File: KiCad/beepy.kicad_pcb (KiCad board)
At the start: 4 copper layers, 74 x 104 mm, 160 parts, among them J1 FDX0019B1, J10 FDX0019B1, J11 FDX0019B1, J12 FDX0019B1, J13 FDX0019B1, J14 FDX0019B1, J15 USB_C_Receptacle_USB2.0, J16 FDX0019B1, J17 FDX0019B1, J18 FDX0019B1, J19 FDX0019B1, J2 FDX0019B1, J20 FDX0019B1, J21 FDX0019B1, J23 FDX0019B1, J24 FDX0019B1, J25 FDX0019B1, J26 FDX0019B1, J27 FDX0019B1, J28 FDX0019B1, J29 FDX0019B1, J3 FDX0019B1, J30 FDX0019B1, J31 FDX0019B1, J32 FDX0019B1, J33 FDX0019B1, J34 FDX0019B1, J35 FDX0019B1, J36 FDX0019B1, J37 FDX0019B1, J38 FDX0019B1, J39 FDX0019B1, J4 FDX0019B1, J40 FDX0019B1, J41 FDX0019B1, J42 FDX0019B1, J43 Battery, J44 Header 1, J45 PRG_HEADER, J46 Header 2, J47 Header 3, J5 FDX0019B1, J6 FDX0019B1, J7 FDX0019B1, J8 FDX0019B1, J9 FDX0019B1, M1 MountingHole_2.5mm_Pad, M2 MountingHole_2.5mm_Pad, M3 MountingHole_2.5mm_Pad, M4 MountingHole_2.5mm_Pad, Q1 SI2301, Q2 SI2301, Q3 BSS138, Q4 BSS138, Q5 BSS138, Q6 BSS138, Q7 BSS138, Q8 BSS138, Q9 S8050, SW1 ON/OFF, SW2 Button, U1 TP4054, U2 TPS61090, U3 LS027B7DH01, U4 AP2112K-3.3, U5 GD25Q16xS, U6 RP2040, U7 ME6212C18M5G, U8 ME6212C28M5G, U9 BBQ20KBD, Y1 XYDBPCNANF-12MHZ

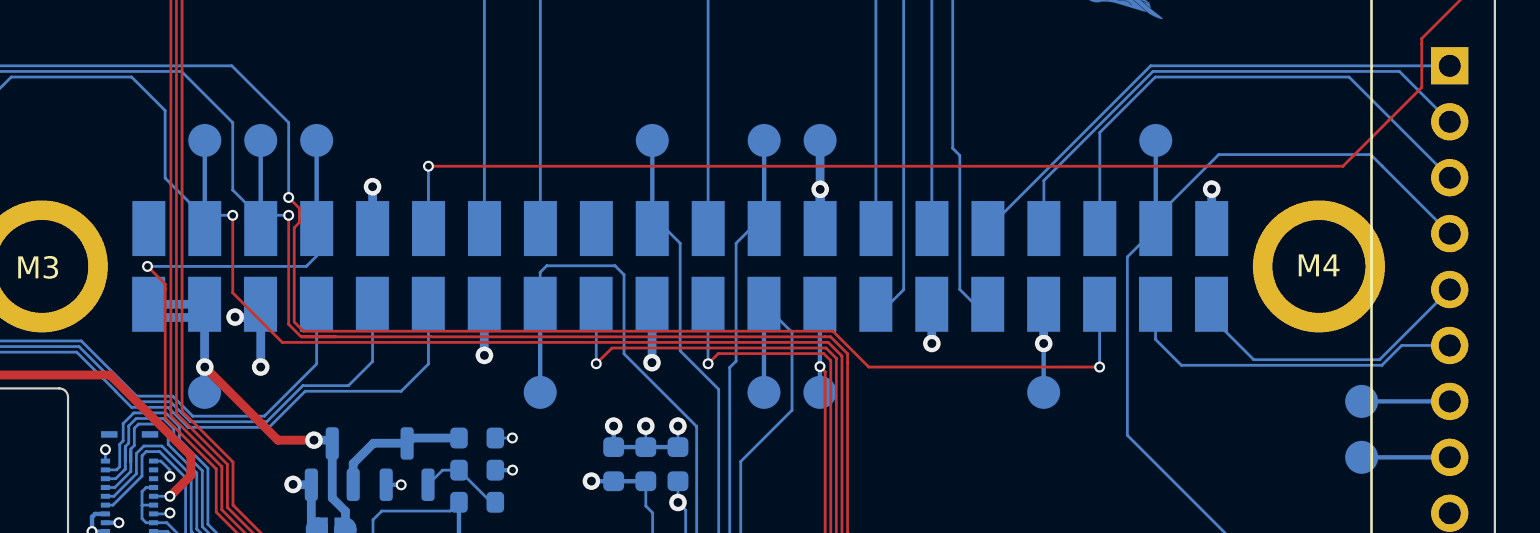
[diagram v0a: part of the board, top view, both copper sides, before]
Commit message: Importing to KiCAD 8 and using pin headers instead of springs
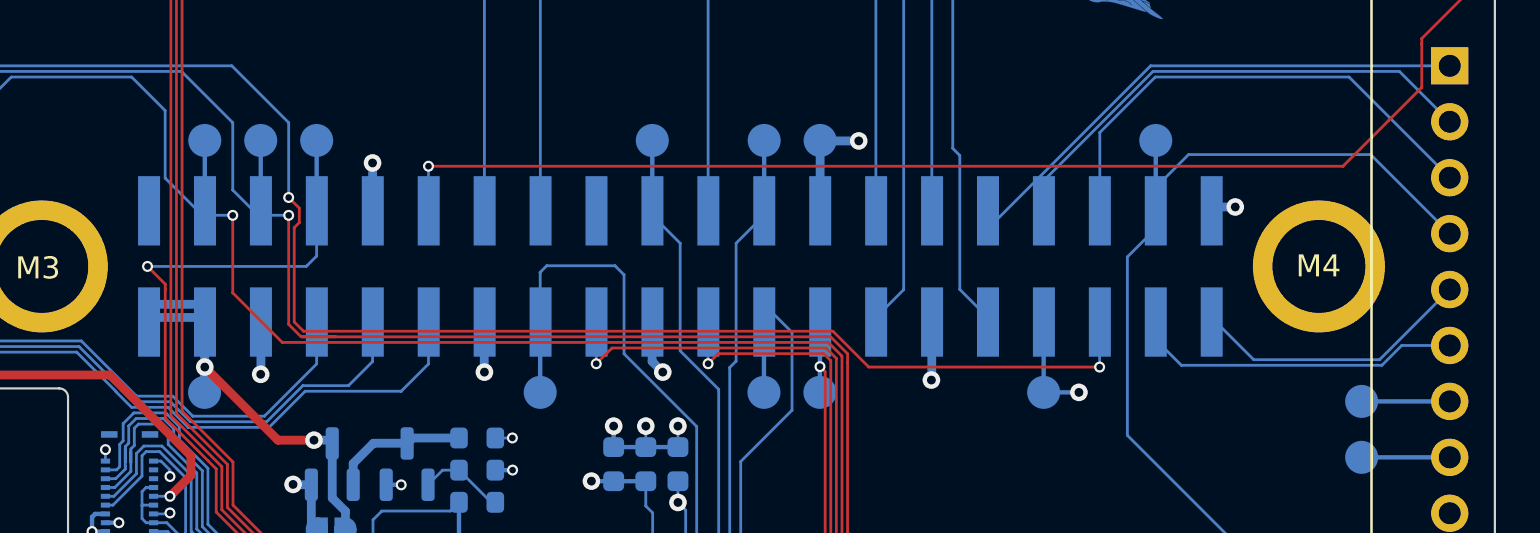
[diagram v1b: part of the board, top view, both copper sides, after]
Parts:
- removed J1, J10, J11, J12, J13, J14, J16, J17, J18, J19, J2, J20, J21, J23, J24, J25, J26, J27, J28, J29, J3, J30, J31, J32, J33, J34, J35, J36, J37, J38, J39, J4, J40, J41, J42, J5, J6, J7, J8, J9: FDX0019B1, beepy:FDX0019B1
- added J22: Pi Zero, Connector_PinHeader_2.54mm:PinHeader_2x20_P2.54mm_Vertical_SMD, B.Cu at (91.1, 69.2)
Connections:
- net /keyboard/BATT_ADC renamed /RP2040/BATT_ADC
- net /keyboard/COL1 renamed /RP2040/COL1
- net /keyboard/COL2 renamed /RP2040/COL2
- net /keyboard/COL3 renamed /RP2040/COL3
- net /keyboard/COL4 renamed /RP2040/COL4
- net /keyboard/COL5 renamed /RP2040/COL5
- net /keyboard/COL6 renamed /RP2040/COL6
- net /keyboard/COL7 renamed /RP2040/COL7
- net /keyboard/D+ renamed /RP2040/D+
- net /keyboard/D- renamed /RP2040/D-
- net /keyboard/KB_BL renamed /RP2040/KB_BL
- net /keyboard/Keyboard/TP_MOTION_1V8 renamed /RP2040/Keyboard/TP_MOTION_1V8
- net /keyboard/Keyboard/TP_RESET_1V8 renamed /RP2040/Keyboard/TP_RESET_1V8
- net /keyboard/Keyboard/TP_SCL_1V8 renamed /RP2040/Keyboard/TP_SCL_1V8
- net /keyboard/Keyboard/TP_SDA_1V8 renamed /RP2040/Keyboard/TP_SDA_1V8
- net /keyboard/Keyboard/TP_SHUTDOWN_1V8 renamed /RP2040/Keyboard/TP_SHUTDOWN_1V8
- net /keyboard/LED_B renamed /RP2040/LED_B
- net /keyboard/LED_G renamed /RP2040/LED_G
- net /keyboard/LED_R renamed /RP2040/LED_R
- net /keyboard/MIC renamed /RP2040/MIC
- net /keyboard/QSPI_SCLK renamed /RP2040/QSPI_SCLK
- net /keyboard/QSPI_SD0 renamed /RP2040/QSPI_SD0
- net /keyboard/QSPI_SD1 renamed /RP2040/QSPI_SD1
- net /keyboard/QSPI_SD2 renamed /RP2040/QSPI_SD2
- net /keyboard/QSPI_SD3 renamed /RP2040/QSPI_SD3
- net /keyboard/ROW1 renamed /RP2040/ROW1
- net /keyboard/ROW2 renamed /RP2040/ROW2
- net /keyboard/ROW3 renamed /RP2040/ROW3
- net /keyboard/ROW4 renamed /RP2040/ROW4
- net /keyboard/ROW5 renamed /RP2040/ROW5
- net /keyboard/ROW6 renamed /RP2040/ROW6
- net /keyboard/ROW7 renamed /RP2040/ROW7
- net /keyboard/TP_MOTION renamed /RP2040/TP_MOTION
- net /keyboard/TP_RESET renamed /RP2040/TP_RESET
- net /keyboard/TP_SCL renamed /RP2040/TP_SCL
- net /keyboard/TP_SDA renamed /RP2040/TP_SDA
- net /keyboard/TP_SHUTDOWN renamed /RP2040/TP_SHUTDOWN
- net /keyboard/~{QSPI_CS} renamed /RP2040/~{QSPI_CS}
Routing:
- net GND: track 104.3 -> 106.5 mm, vias 58 -> 57
- net /Pi_GPIO26: track 80.6 -> 81.4 mm
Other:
- board text added: "REF**"
- board text removed: "locked"

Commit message: Moving header designator
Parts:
- U5: value GD25Q16xS -> W25Q16JVSSIQ
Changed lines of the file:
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@@
 			)
 		)
-		(property "Value" "GD25Q16xS"
+		(property "Value" "W25Q16JVSSIQ"
 			(at 0 -3.57 0)
 			(layer "B.Fab")
@@
 			)
 		)
-		(property "LCSC" "C79074"
+		(property "LCSC" "C131025"
 			(at 0 0 0)
 			(layer "B.Fab")
@@
 		(tags "Surface mounted pin header SMD 2x20 2.54mm double row")
 		(property "Reference" "J22"
-			(at 0 26.46 90)
-			(layer "B.SilkS")
-			(effects
+			(at -4.4 26.1 90)
+			(layer "B.SilkS")
+			(effects
